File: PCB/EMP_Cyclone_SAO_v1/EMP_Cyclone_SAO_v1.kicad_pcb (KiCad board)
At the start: 2 copper layers, 101 x 86 mm, 8 parts, among them SW1 SW_Push, SW2 SW_Push, SW3 SW_Push

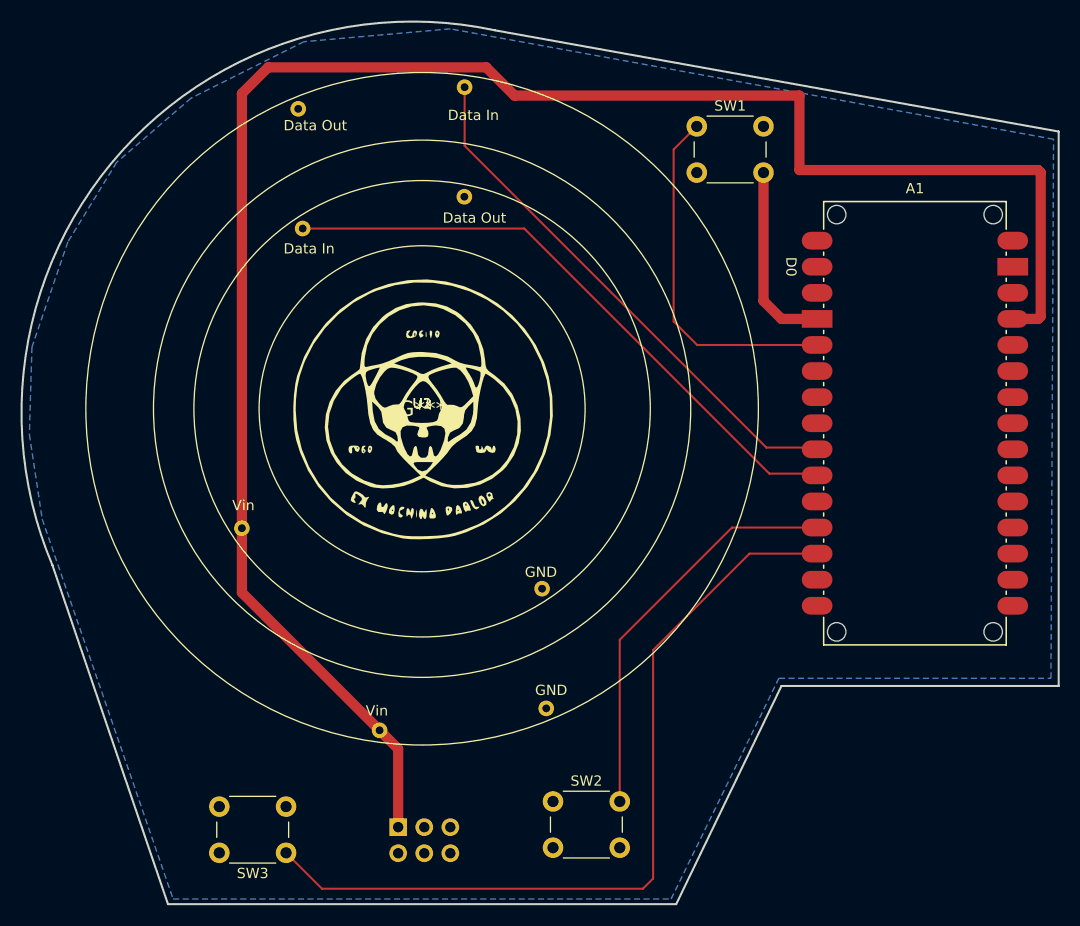
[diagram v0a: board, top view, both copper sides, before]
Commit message: v1. Updated silk screen on pcb. minor changes to traces. Updated gerber files.
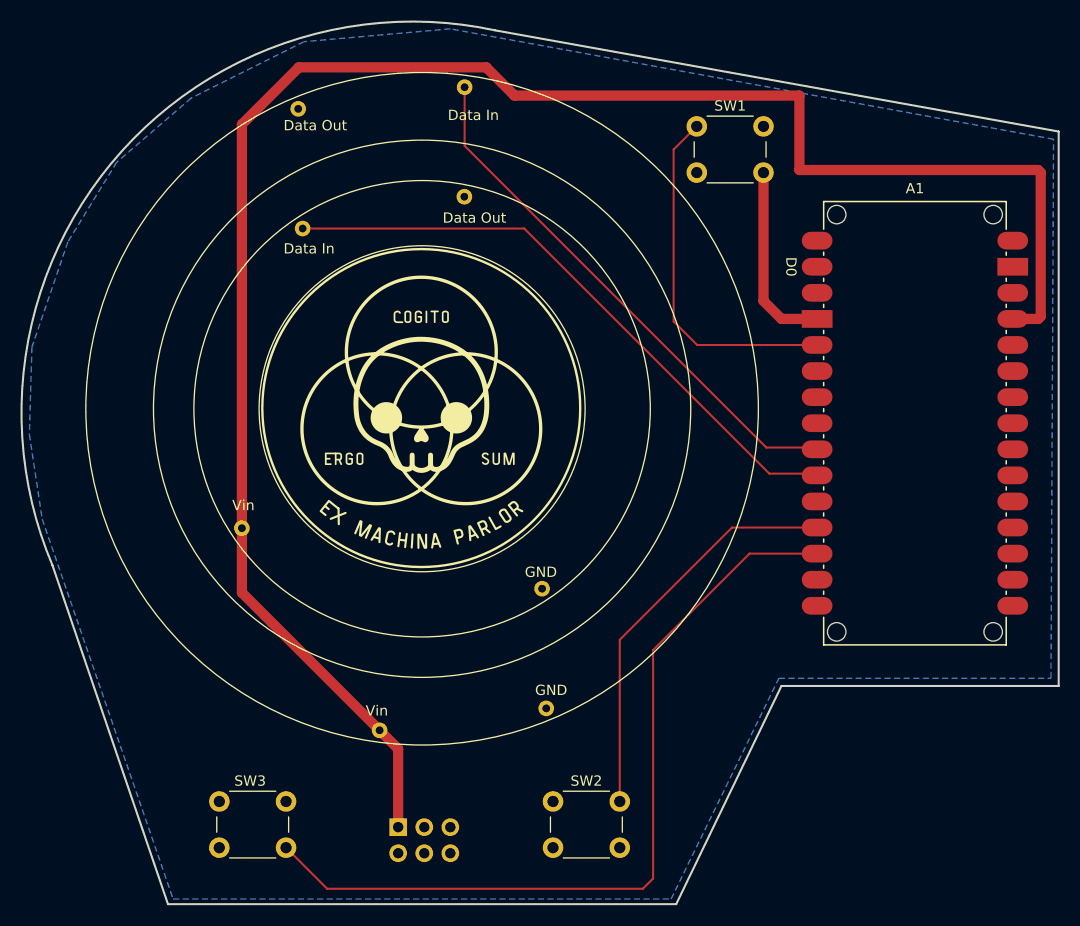
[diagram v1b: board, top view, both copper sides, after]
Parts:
- removed the G*** at (100.0, 100.0)
- added G***: LOGO, LOGO, B.Cu at (147.8, 106.8)
- moved SW3 0.50 mm to (86.8, 142.8)
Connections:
- A1 pad D10: (no net) -> Net-(A1-D10)
- A1 pad D2: (no net) -> Net-(A1-D2)
- A1 pad D9: (no net) -> Net-(A1-D9)
- A1 pad GND1: (no net) -> GND
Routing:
- net (no net): track 294.9 -> 293.1 mm
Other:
- board text added: "CMc"
- board text added: "EMP Cyclone SAO PCB v1"

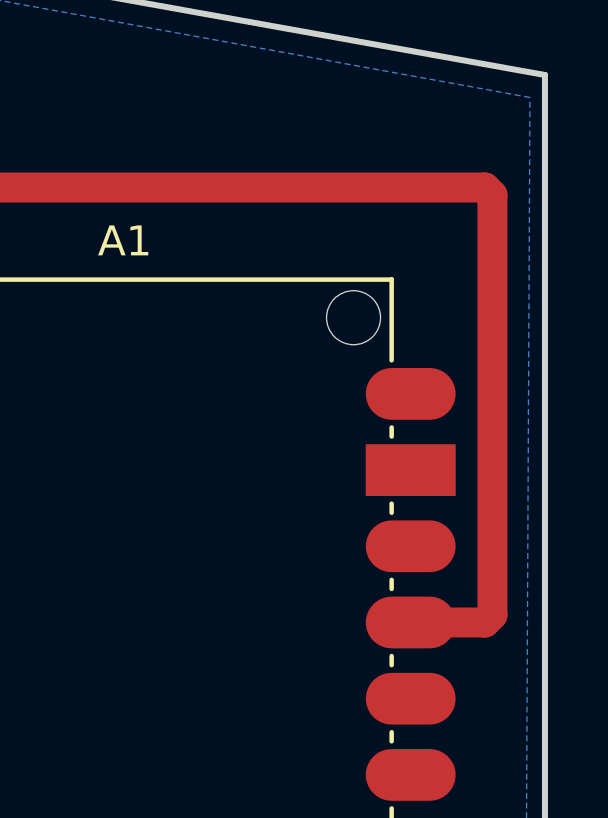
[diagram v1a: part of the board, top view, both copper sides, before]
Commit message: Tested working on v1 PCB. Updated arduino sketch for pins used on v1 PCB. Minor updates to PCB silkscreen.
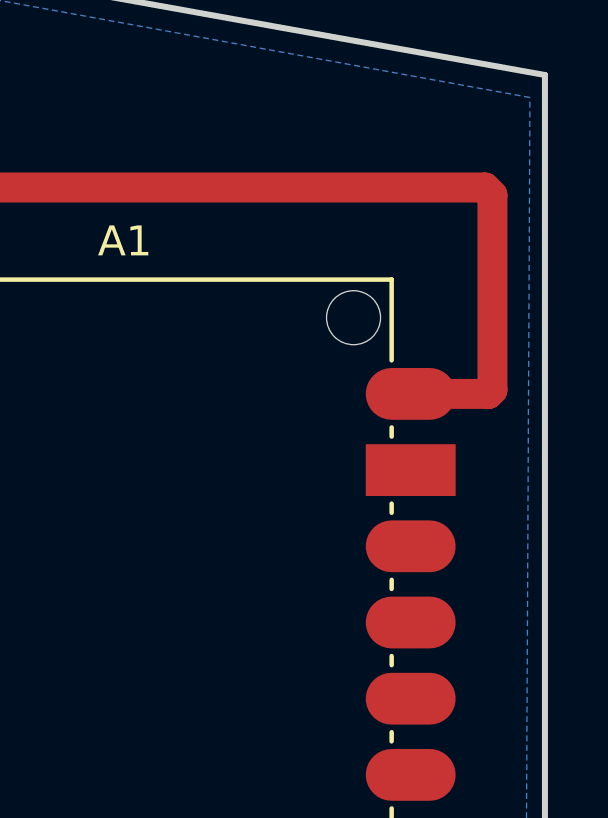
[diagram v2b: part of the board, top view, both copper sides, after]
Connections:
- U1 pad 4: (no net) -> GND
- U2 pad 4: (no net) -> GND
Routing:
- net (no net): track 293.1 -> 285.5 mm
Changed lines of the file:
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@@
 			(layers "*.Cu" "*.Mask")
 			(remove_unused_layers no)
+			(net 1 "GND")
 		)
 	)
@@
 			(layers "*.Cu" "*.Mask")
 			(remove_unused_layers no)
+			(net 1 "GND")
 		)
 	)
@@
 	)
 	(segment
-		(start 97.67 133.1284)
-		(end 95.8598 131.3182)
+		(start 160.25 83.5)
+		(end 160.12 83.63)
 		(width 1)
 		(layer "F.Cu")
@@
 	)
 	(segment
-		(start 160.25 91)
-		(end 160.25 77)
+		(start 97.67 133.1284)
+		(end 95.8598 131.3182)
 		(width 1)
 		(layer "F.Cu")
@@
 	)
 	(segment
-		(start 157.42 91.25)
-		(end 160 91.25)
+		(start 160.12 83.63)
+		(end 157.525 83.63)
 		(width 1)
 		(layer "F.Cu")
@@
 	)
 	(segment
-		(start 160 91.25)
-		(end 160.25 91)
-		(width 1)
-		(layer "F.Cu")
-		(net 0)
-	)
-	(segment
 		(start 138.305 116.48)
 		(end 138.475 116.65)
@@
 		(width 1)
 		(layer "F.Cu")
+		(net 0)
+	)
+	(segment
+		(start 160.25 77)
+		(end 160.25 83.5)
+		(width 1)
+		(layer "F.Cu")

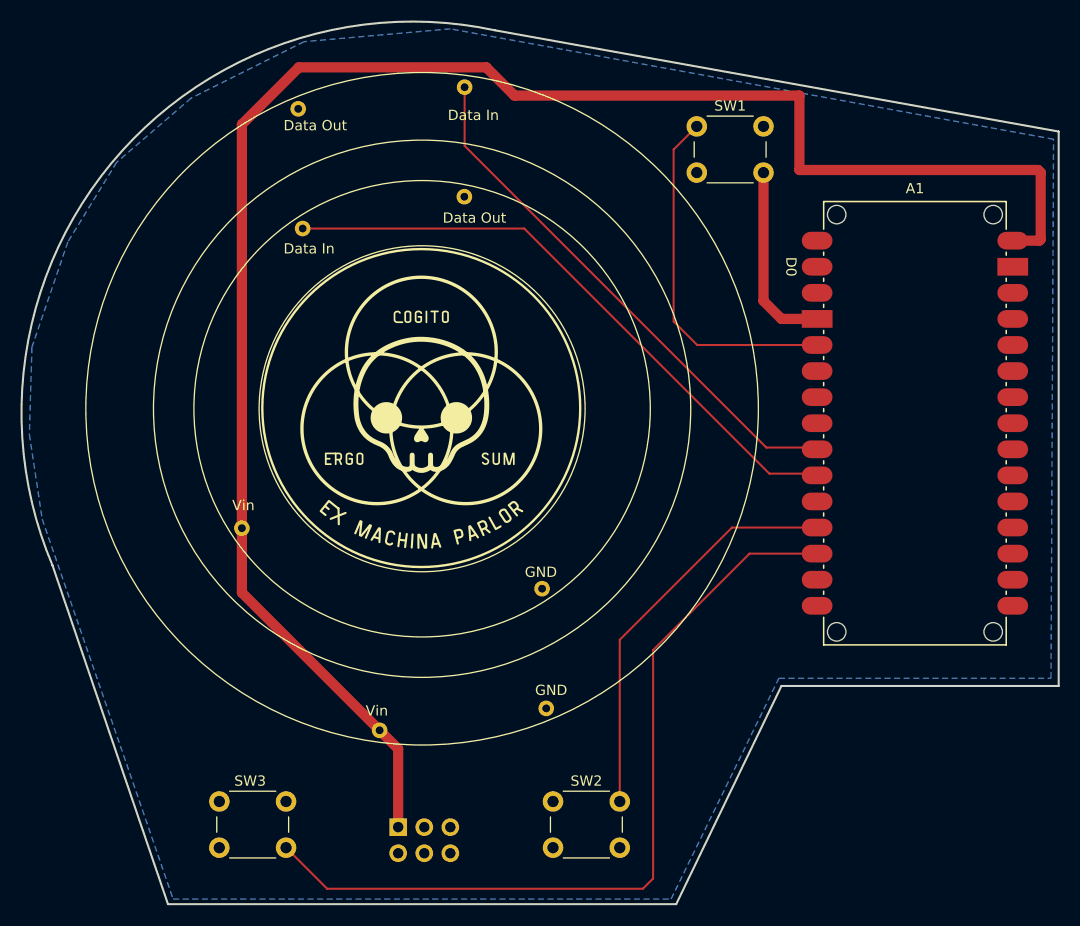
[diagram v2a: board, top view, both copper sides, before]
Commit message: updated to use ESP32-C3 supermini
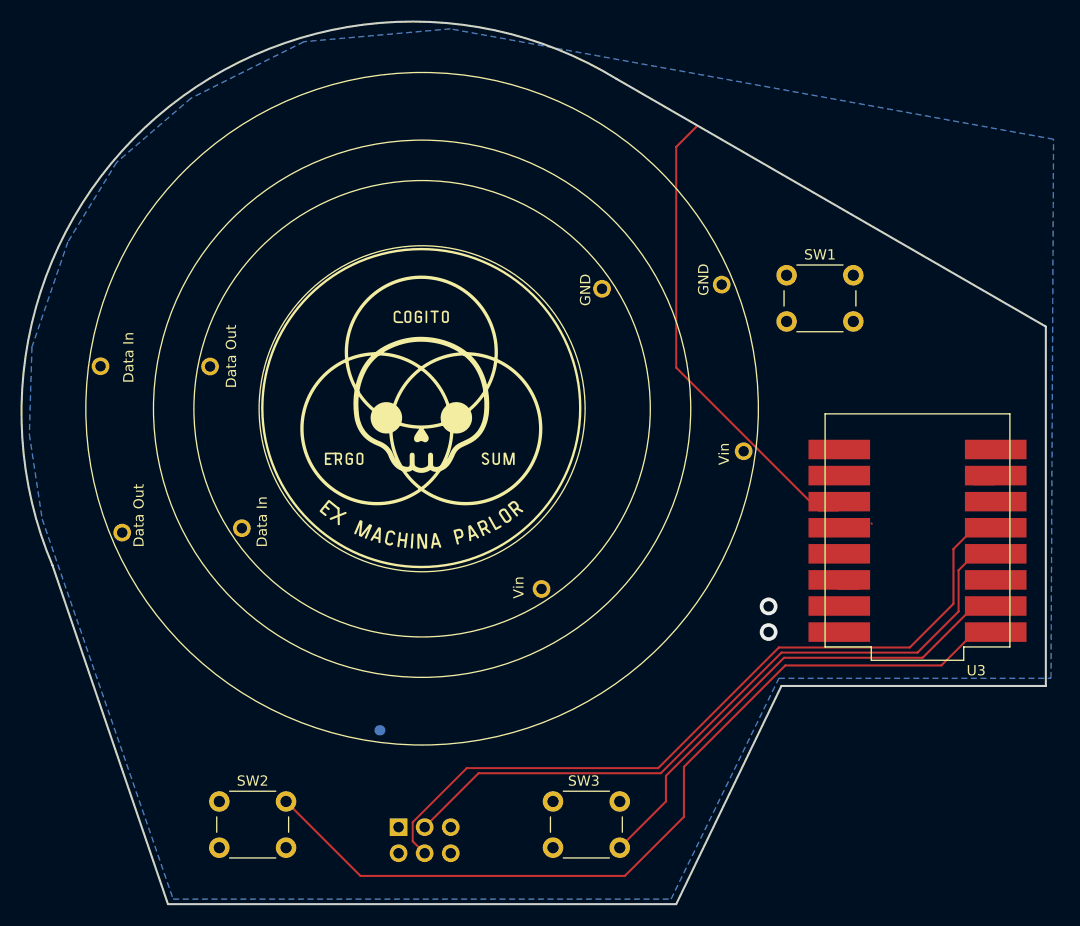
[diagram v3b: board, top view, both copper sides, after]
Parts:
- removed A1: Arduino_Nano_Every, PCM_arduino-library:Arduino_Nano_Every_Tile
- added U3: ESP32-C3_SUPERMINI, neopixelrings-2:MODULE_ESP32-C3_SUPERMINI, F.Cu at (148.2, 111.8)
- moved SW2 32.5 mm to (80.2, 138.2)
- moved SW3 32.5 mm to (119.2, 142.8)
- moved SW1 16.9 mm to (135.5, 87.0)
- turned U1 to 90 degrees
- turned U2 to 90 degrees
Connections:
- REF** pad 1: (no net) -> +5V
- REF** pad 3: (no net) -> unconnected-(U3-GPIO8-Pad8)
- REF** pad 4: (no net) -> unconnected-(U3-GPIO9-Pad9)
- U1 pad 3: (no net) -> +5V
- U1 pad 4: GND -> (no net)
- U2 pad 3: (no net) -> +5V
- U2 pad 4: GND -> (no net)
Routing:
- net (no net): track 285.5 -> 0.00 mm
- net unconnected-(U3-GPIO9-Pad9): track 0.00 -> 75.3 mm
- net unconnected-(U3-GPIO8-Pad8): track 0.00 -> 69.0 mm
- net Net-(U2-Data_In): track 0.00 -> 45.8 mm
- net Net-(U3-GPIO5): track 39.5 -> 84.8 mm
- net Net-(U3-GPIO4): track 34.9 -> 0.00 mm
- net Net-(U3-GPIO6): track 80.2 -> 47.8 mm
- net GND: track 18.4 -> 0.25 mm, vias 0 -> 1
- net unconnected-(U3-GPIO20-Pad20): track 0.00 -> 2.05 mm
- net unconnected-(U3-3V3-Pad3.3): track 0.00 -> 2.05 mm
- net +5V: track 0.00 -> 0.11 mm, vias 0 -> 1
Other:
- board size 101 x 86 mm -> 99.8 x 86 mm

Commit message: v1.1 in progress with ESP32-C3 moved to back
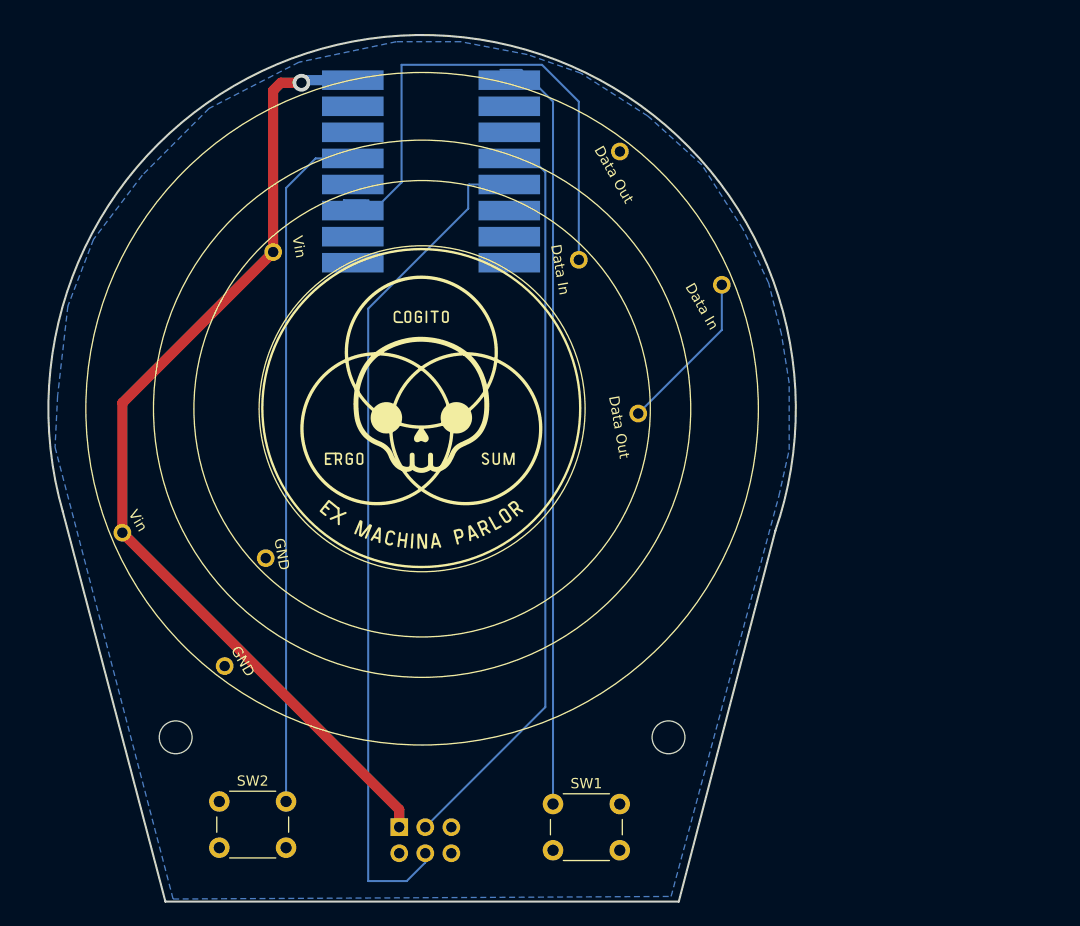
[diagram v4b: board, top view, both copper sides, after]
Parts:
- removed SW3: SW_Push, Button_Switch_THT:SW_PUSH_6mm
- U3: moved to B.Cu
- moved U3 58.3 mm to (100.9, 77.9)
- moved SW1 56.3 mm to (112.8, 138.5)
- moved G*** 50.9 mm to (100.2, 125.0)
- moved REF** 0.06 mm to (100.2, 142.0)
- turned U1 to -80 degrees
- turned U2 to -60 degrees
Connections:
- SW1 pad 1: Net-(U3-GPIO4) -> Net-(U3-GPIO5)
- SW2 pad 1: Net-(U3-GPIO5) -> Net-(U3-GPIO4)
- U1 pad 1: (no net) -> Net-(U2-Data_In)
- U1 pad 4: (no net) -> GND
- U2 pad 4: (no net) -> GND
- U3 pad 6: Net-(U3-GPIO6) -> unconnected-(U3-GPIO6-Pad6)
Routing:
- net +5V: track 0.11 -> 97.2 mm
- net Net-(U3-GPIO4): track 0.00 -> 67.4 mm
- net Net-(U3-GPIO6): track 47.8 -> 0.00 mm
- net (no net): track 0.00 -> 15.9 mm
- net Net-(U2-Data_In): track 45.8 -> 56.1 mm
- net Net-(U3-GPIO5): track 84.8 -> 74.8 mm
- net unconnected-(U3-GPIO9-Pad9): track 75.3 -> 83.0 mm
- net unconnected-(U3-GPIO8-Pad8): track 69.0 -> 72.7 mm
- net unconnected-(U3-GPIO20-Pad20): track 2.05 -> 0.00 mm
- net unconnected-(U3-3V3-Pad3.3): track 2.05 -> 0.00 mm
- net GND: vias 1 -> 0
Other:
- board size 99.8 x 86 mm -> 72.8 x 84.4 mm
- board text added: "EMP Cyclone SAO PCB v2"
- board text removed: "EMP Cyclone SAO PCB v1"
